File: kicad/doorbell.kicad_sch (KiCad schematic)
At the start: 93 parts, among them J1 USB-C (USB4105), J2 WF26 bus, K1 GAQW212GS, K2 GAQY212GS, K3 GAQY412EH, K4 GAQY412EH, K5 G6K-2F-Y DC12, Q3 2N7002, Q4 2N7002, SW1 BOOT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

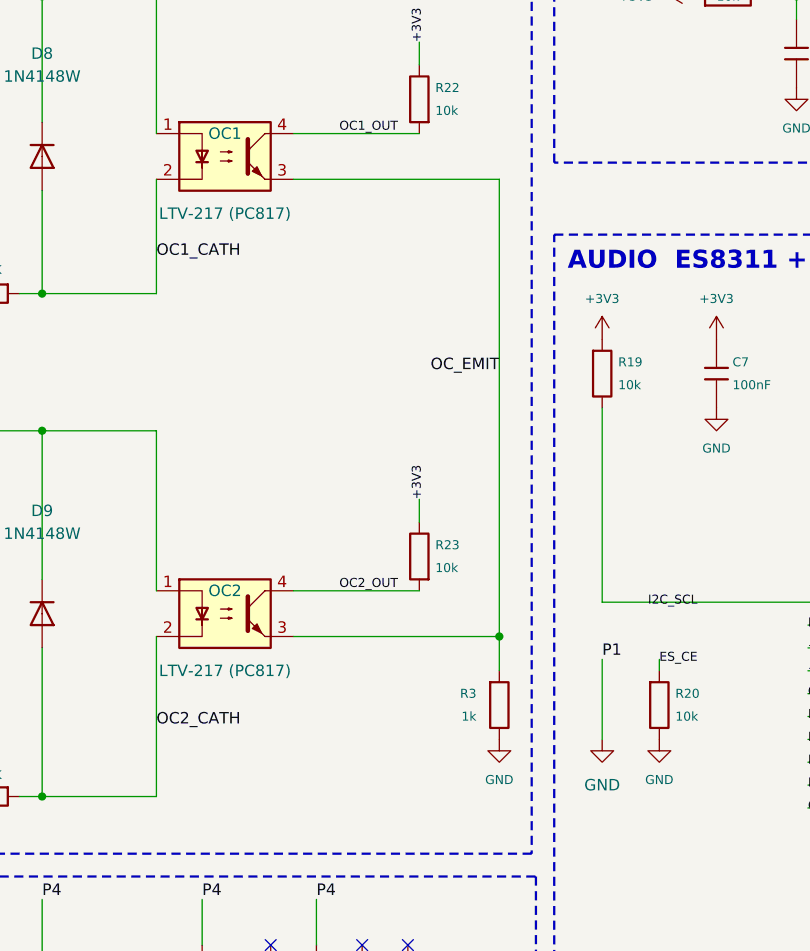
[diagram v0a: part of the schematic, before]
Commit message: kicad: drop R3 shared opto-emitter R, tie OC1/OC2 emitters direct to GND
Removes the 1k shared emitter return for OC1+OC2 (prefab W3). In the
simultaneous-ring corner (front-door Türruf overlapping an apartment Etagenruf
tone) each saturated phototransistor sinks ~0.27 mA, lifting the shared node
~0.54 V and pushing each GPIO LOW to ~0.63-0.91 V — touching the ESP V_IL at
the +5% supply corner. Routing each emitter straight to GND drops every LOW
back to Vce(sat) with no shared node, so detection holds regardless of how many
bells ring at once. PCB rerouted + zones refilled.

Claude-Session: https://claude.ai/code/session_01L7QeT64g2akf3TXKfsuiUZ
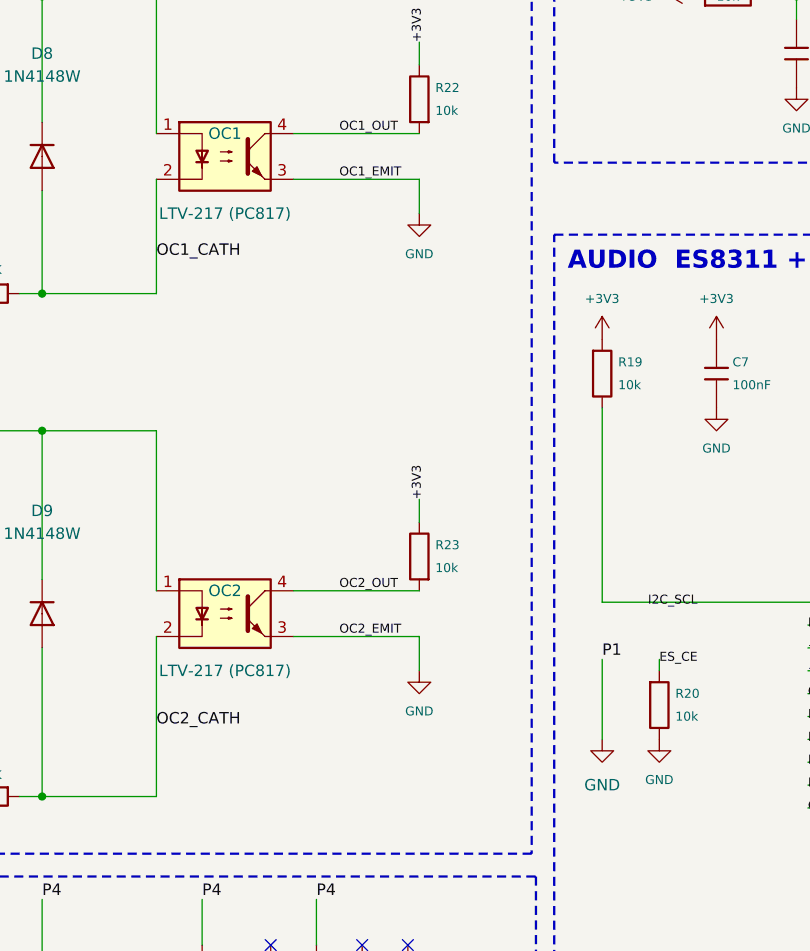
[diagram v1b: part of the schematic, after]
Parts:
- removed R3: 1k, PCM_JLCPCB:R_0603, symbol PCM_JLCPCB-Resistors:0603,1kΩ
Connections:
- net OC_EMIT is gone; now on net GND: OC1.3, OC2.3
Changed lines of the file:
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@@
 	)
 	(junction
-		(at 152.4 184.15)
-		(diameter 0)
-		(color 0 0 0 0)
-	)
-	(junction
 		(at 87.63 247.65)
 		(diameter 0)
@@
 	(wire
 		(pts
-			(xy 152.4 133.35) (xy 152.4 184.15)
-		)
-		(stroke
-			(width 0)
-			(type default)
-		)
-	)
-	(wire
-		(pts
 			(xy 260.35 185.42) (xy 260.35 215.9)
 		)
@@
 	(wire
 		(pts
-			(xy 129.54 184.15) (xy 152.4 184.15)
+			(xy 129.54 184.15) (xy 143.51 184.15)
 		)
 		(stroke
@@
 	(wire
 		(pts
+			(xy 129.54 133.35) (xy 143.51 133.35)
+		)
+		(stroke
+			(width 0)
+			(type default)
+		)
+	)
+	(wire
+		(pts
 			(xy 251.46 190.5) (xy 247.65 190.5)
 		)
@@
 	(wire
 		(pts
+			(xy 143.51 133.35) (xy 143.51 137.16)
+		)
+		(stroke
+			(width 0)
+			(type default)
+		)
+	)
+	(wire
+		(pts
 			(xy 360.68 82.55) (xy 365.76 82.55)
 		)
@@
 	(wire
 		(pts
-			(xy 129.54 133.35) (xy 152.4 133.35)
-		)
-		(stroke
-			(width 0)
-			(type default)
-		)
-	)
-	(wire
-		(pts
 			(xy 119.38 240.03) (xy 119.38 233.68)
 		)
@@
 	(wire
 		(pts
-			(xy 152.4 184.15) (xy 152.4 187.96)
+			(xy 143.51 184.15) (xy 143.51 187.96)
 		)
 		(stroke
@@
 		)
 	)
+	(label "OC2_EMIT"
+		(at 134.62 184.15 0)
+		(effects
+			(font
+				(size 1 1)
+			)
+			(justify bottom)
+		)
+	)
 	(label "+3V3"
 		(at 186.69 185.42 0)
@@
 		)
 	)
-	(label "OC_EMIT"
-		(at 152.4 154.94 180)
-		(effects
-			(font
-				(size 1.27 1.27)
-			)
-			(justify right bottom)
-		)
-	)
 	(label "OC2_CATH"
 		(at 114.3 194.31 0)
@@
 		)
 	)
+	(label "OC1_EMIT"
+		(at 134.62 133.35 0)
+		(effects
+			(font
+				(size 1 1)
+			)
+			(justify bottom)
+		)
+	)
 	(label "OC1_CATH"
 		(at 114.3 142.24 0)
@@
 	)
 	(symbol
+		(lib_id "power:GND")
+		(at 143.51 137.16 0)
+		(mirror y)
+		(unit 1)
+		(body_style 1)
+		(exclude_from_sim no)
+		(in_bom no)
+		(on_board no)
+		(in_pos_files yes)
+		(dnp no)
+		(property "Reference" "#PWR056"
+			(at 143.51 137.16 0)
+			(hide yes)
+			(show_name no)
+			(do_not_autoplace no)
+			(effects
+				(font
+					(size 1 1)
+				)
+			)
+		)
+		(property "Value" "GND"
+			(at 143.51 141.66 0)
+			(show_name no)
+			(do_not_autoplace no)
+			(effects
+				(font
+					(size 1 1)
+				)
+			)
+		)
+		(property "Footprint" ""
+			(at 143.51 137.16 0)
+			(show_name no)
+			(do_not_autoplace no)
+			(effects
+				(font
+					(size 1.27 1.27)
+				)
+			)
+		)
+		(property "Datasheet" ""
+			(at 143.51 137.16 0)
+			(show_name no)
+			(do_not_autoplace no)
+			(effects
+				(font
+					(size 1.27 1.27)
+				)
+			)
+		)
+		(property "Description" ""
+			(at 143.51 137.16 0)
+			(show_name no)
+			(do_not_autoplace no)
+			(effects
+				(font
+					(size 1.27 1.27)
+				)
+			)
+		)
+		(pin "1"
+		)
+		(instances
+			(project "doorbell"
+				(path "/959c5810-086a-4a51-98b0-f68b22907a4f"
+					(reference "#PWR056")
+					(unit 1)
+				)
+			)
+		)
+	)
+	(symbol
 		(lib_id "PCM_JLCPCB-Resistors:0603,22kΩ")
 		(at 242.57 220.98 0)
@@
 	(symbol
 		(lib_id "power:GND")
-		(at 152.4 195.58 0)
+		(at 143.51 187.96 0)
 		(unit 1)
 		(body_style 1)
@@
 		(dnp no)
 		(property "Reference" "#PWR34"
-			(at 152.4 195.58 0)
+			(at 143.51 187.96 0)
 			(hide yes)
 			(show_name no)
@@
 		)
 		(property "Value" "GND"
-			(at 152.4 200.08 0)
+			(at 143.51 192.46 0)
 			(show_name no)
 			(do_not_autoplace no)
@@
 		)
 		(property "Footprint" ""
-			(at 152.4 195.58 0)
+			(at 143.51 187.96 0)
 			(show_name no)
 			(do_not_autoplace no)
@@
 		)
 		(property "Datasheet" ""
-			(at 152.4 195.58 0)
+			(at 143.51 187.96 0)
 			(show_name no)
 			(do_not_autoplace no)
@@
 		)
 		(property "Description" ""
-			(at 152.4 195.58 0)
+			(at 143.51 187.96 0)
 			(show_name no)
 			(do_not_autoplace no)
@@
 					(unit 1)
 				)
-			)
-		)
-	)
-	(symbol
-		(lib_id "PCM_JLCPCB-Resistors:0603,1kΩ")
-		(at 152.4 191.77 0)
-		(unit 1)
-		(body_style 1)
-		(exclude_from_sim no)
-		(in_bom yes)
-		(on_board yes)
-		(in_pos_files yes)
-		(dnp no)
-		(property "Reference" "R3"
-			(at 149.86 190.5 0)
-			(show_name no)
-			(do_not_autoplace no)
-			(effects
-				(font
-					(size 1 1)
-				)
-				(justify right)
-			)
-		)
-		(property "Value" "1k"
-			(at 149.86 193.04 0)
-			(show_name no)
-			(do_not_autoplace no)
-			(effects
-				(font
-					(size 1 1)
-				)
-				(justify right)
-			)
-		)
-		(property "Footprint" "PCM_JLCPCB:R_0603"
-			(at 152.4 191.77 0)
-			(hide yes)
-			(show_name no)
-			(do_not_autoplace no)
-			(effects
-				(font
-					(size 1 1)
-				)
-			)
-		)
-		(property "Datasheet" "https://www.lcsc.com/datasheet/lcsc_datasheet_2206010130_UNI-ROYAL-Uniroyal-Elec-0603WAF1001T5E_C21190.pdf"
-			(at 152.4 191.77 0)
-			(hide yes)
-			(show_name no)
-			(do_not_autoplace no)
-			(effects
-				(font
-					(size 1 1)
-				)
-			)
-		)
-		(property "Description" "Shared opto emitter resistor to GND (uA only)"
-			(at 152.4 191.77 0)
-			(hide yes)
-			(show_name no)
-			(do_not_autoplace no)
-			(effects
-				(font
-					(size 1 1)
-				)
-			)
-		)
-		(property "LCSC" "C21190"
-			(at 152.4 191.77 0)
-			(hide yes)
-			(show_name no)
-			(do_not_autoplace no)
-			(effects
-				(font
-					(size 1 1)
-				)
-			)
-		)
-		(property "MPN" "0603WAF1001T5E"
-			(at 152.4 191.77 0)
-			(hide yes)
-			(show_name no)
-			(do_not_autoplace no)
-			(effects
-				(font
-					(size 1 1)
-				)
-			)
-		)
-		(pin "1"
-		)
-		(pin "2"
-		)
-		(instances
-			(project "doorbell"
-				(path "/959c5810-086a-4a51-98b0-f68b22907a4f"
-					(reference "R3")
-					(unit 1)
-				)

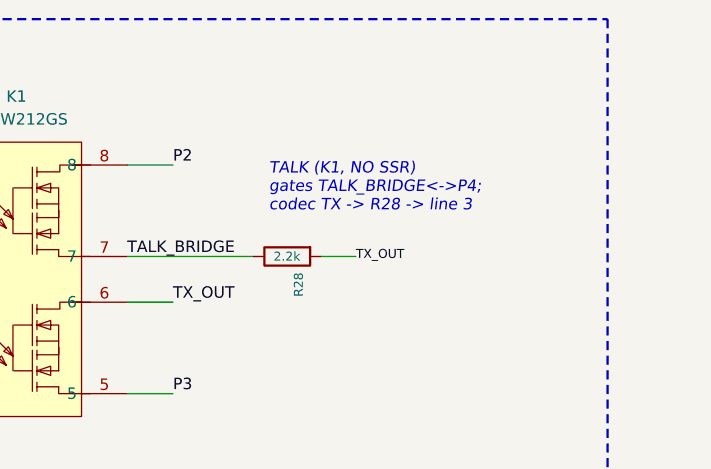
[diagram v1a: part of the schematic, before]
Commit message: kicad: fix W5 doc/tooling drift (TALK annotation + check_pcb no-connect)
- sch: TALK gate annotation TALK_BRIDGE<->P4 -> P2 (matches K1 pole-A nets and its
  own Description); regenerate doorbell.pdf
- doorbell_design.py: drop the vestigial REF identity map and the stale, inert NOCONN
  whitelist. All relay/SSR pads are netted (K1=AQW212 dual, K2/K3=AQY212/AQY412);
  KiCad already names intended no-connects unconnected-(...).
- check_pcb.py: flag any empty-net copper pad directly -- keeps the netlist-omission
  guard with no hand-maintained list; NC intent stays in the schematic's NC flags.
- DESIGN.md / kicad/README.md: correct the doorbell_design.py description (no LCSC
  dict or refdes map; only check_pcb.py imports it; LCSC lives in the schematic symbols).
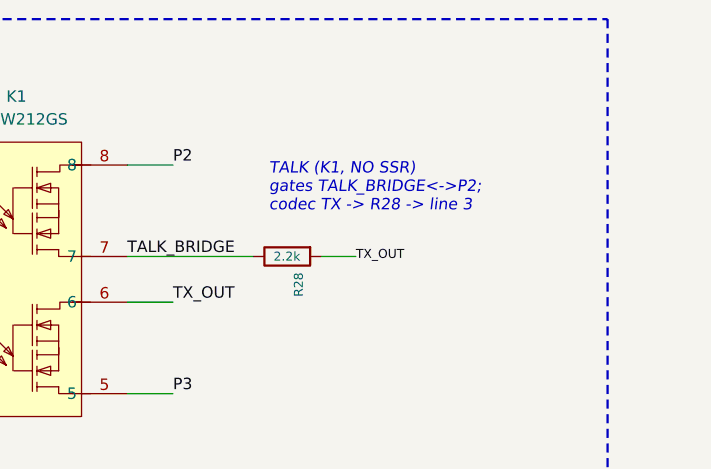
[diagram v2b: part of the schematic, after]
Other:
- note added: "TALK (K1, NO SSR) gates TALK_BRIDGE<->P2; codec TX -> R28 -> line 3"
- note removed: "TALK (K1, NO SSR) gates TALK_BRIDGE<->P4; codec TX -> R28 -> line 3"
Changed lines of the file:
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@@
 		)
 	)
-	(text "TALK (K1, NO SSR)\ngates TALK_BRIDGE<->P4;\ncodec TX -> R28 -> line 3"
+	(text "TALK (K1, NO SSR)\ngates TALK_BRIDGE<->P2;\ncodec TX -> R28 -> line 3"
 		(exclude_from_sim no)
 		(at 357.378 31.75 0)

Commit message: kicad: correct TALK annotation (P2 -> P4)
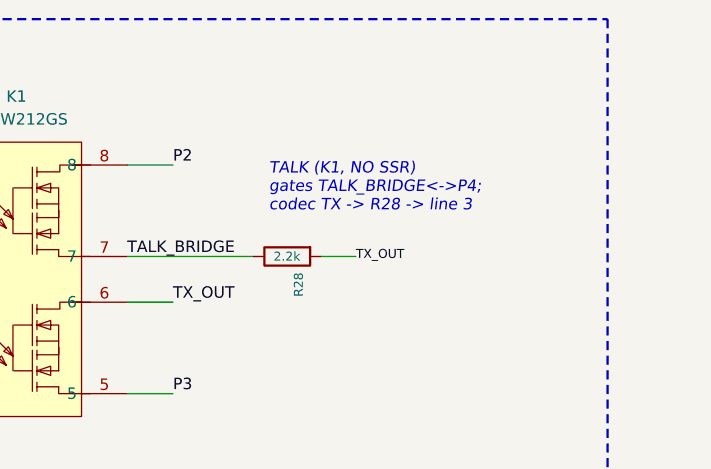
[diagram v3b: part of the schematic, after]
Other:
- note added: "TALK (K1, NO SSR) gates TALK_BRIDGE<->P4; codec TX -> R28 -> line 3"
- note removed: "TALK (K1, NO SSR) gates TALK_BRIDGE<->P2; codec TX -> R28 -> line 3"
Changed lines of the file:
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@@
 		)
 	)
-	(text "TALK (K1, NO SSR)\ngates TALK_BRIDGE<->P2;\ncodec TX -> R28 -> line 3"
+	(text "TALK (K1, NO SSR)\ngates TALK_BRIDGE<->P4;\ncodec TX -> R28 -> line 3"
 		(exclude_from_sim no)
 		(at 357.378 31.75 0)

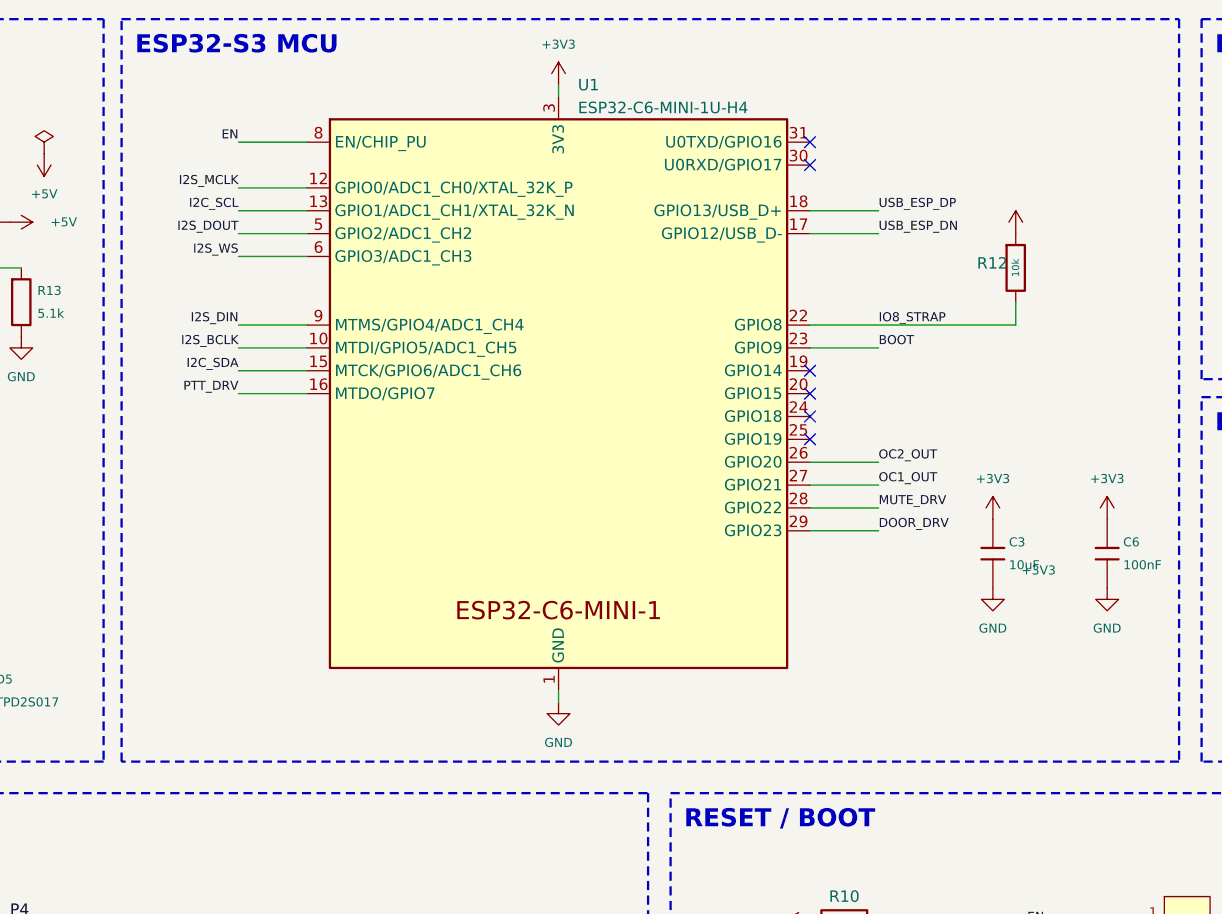
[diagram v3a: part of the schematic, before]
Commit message: kicad+fw+docs: migrate V4 from ESP32-C6 to ESP32-S3-WROOM-1U-N16R8
The single-core C6 starves its WiFi RX under sustained audio load
(pcap-confirmed stream stalls), so audio-over-WiFi never settles. The
dual-core S3 + 8 MB octal PSRAM gives the headroom: audio buffers live in
PSRAM off the internal SRAM, and the WiFi/TLS stack and audio pipeline run
on separate cores.

- kicad: swap U1 ESP32-C6-MINI-1U -> ESP32-S3-WROOM-1U-N16R8 (16 MB flash,
  8 MB PSRAM, u.FL), rewire to the S3 pinout, drop R12, place + reposition
  for the spin. S3 3D model added under kicad/lib_mcu/.
- firmware/doorbell-v4.yaml: board esp32-s3-devkitc-1 / variant esp32s3,
  flash_size 16MB, add psram (octal 80MHz), remap all I2C/I2S/SSR/opto pins.
- DESIGN.md: MCU rationale, GPIO map, V3<->V4 table, and C6/MINI-1U refs
  updated to the S3.

Claude-Session: https://claude.ai/code/session_01L7QeT64g2akf3TXKfsuiUZ
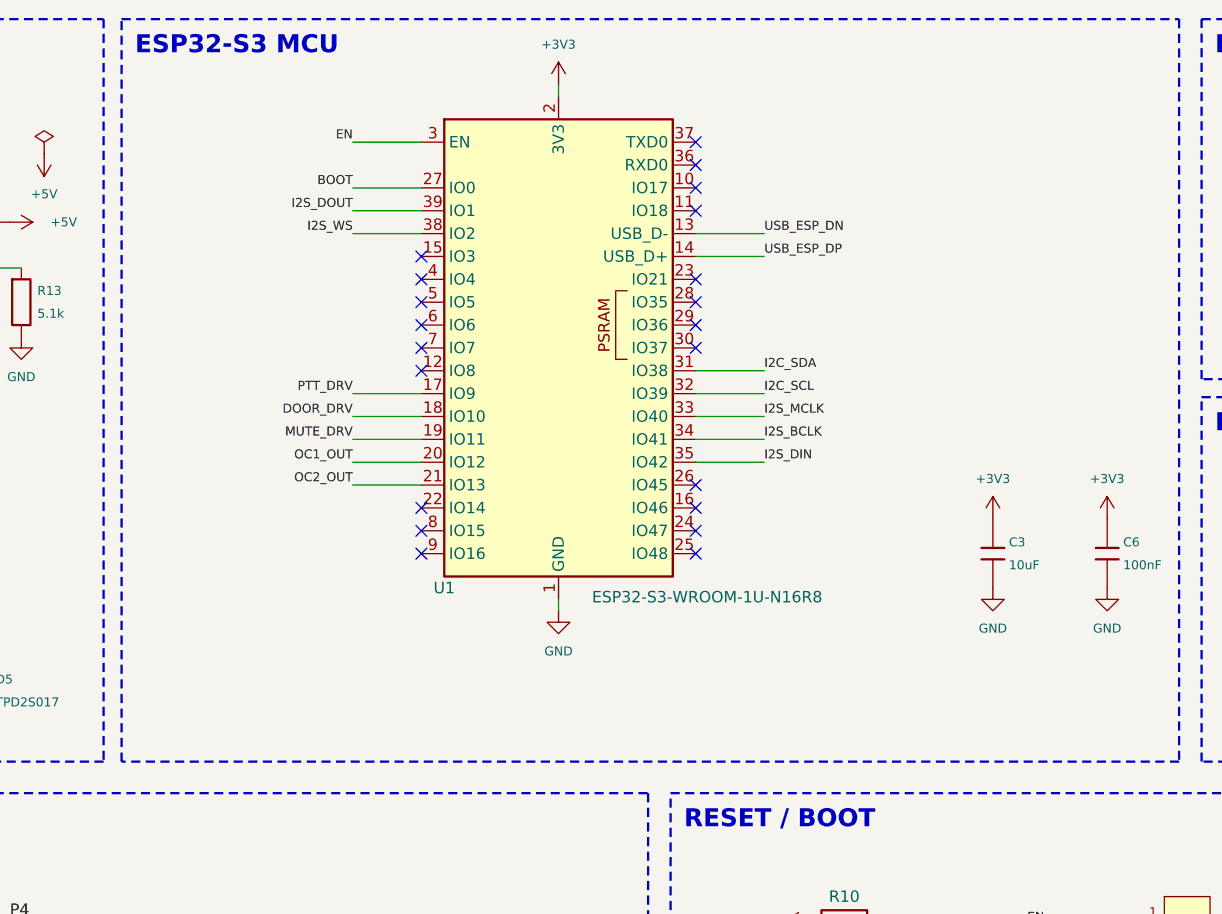
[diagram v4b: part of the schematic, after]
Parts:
- removed R12: 10k, PCM_JLCPCB:R_0402, symbol PCM_JLCPCB-Resistors:0603,10kΩ
- removed U1: ESP32-C6-MINI-1U-H4, PCM_Espressif:ESP32-C6-MINI-1U, symbol PCM_Espressif:ESP32-C6-MINI-1/U
- added U1: ESP32-S3-WROOM-1U-N16R8, RF_Module:ESP32-S3-WROOM-1U, symbol RF_Module:ESP32-S3-WROOM-1
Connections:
- net +3V3: now also U1.2 (3V3)
- net BOOT: now also U1.27 (IO0)
- net DOOR_DRV: now also U1.18 (IO10)
- net EN: now also U1.3 (EN)
- net GND: now also U1.1 (GND), U1.40 (GND), U1.41 (GND)
- net I2C_SCL: now also U1.32 (IO39)
- net I2C_SDA: now also U1.31 (IO38)
- net I2S_BCLK: now also U1.34 (IO41)
- net I2S_DIN: now also U1.35 (IO42)
- net I2S_DOUT: now also U1.39 (IO1)
- net I2S_MCLK: now also U1.33 (IO40)
- net I2S_WS: now also U1.38 (IO2)
- net MUTE_DRV: now also U1.19 (IO11)
- net OC1_OUT: now also U1.20 (IO12)
- net OC2_OUT: now also U1.21 (IO13)
- net PTT_DRV: now also U1.17 (IO9)
- net USB_ESP_DN: now also U1.13 (USB_D-)
- net USB_ESP_DP: now also U1.14 (USB_D+)
- no-connect marks 14 -> 29

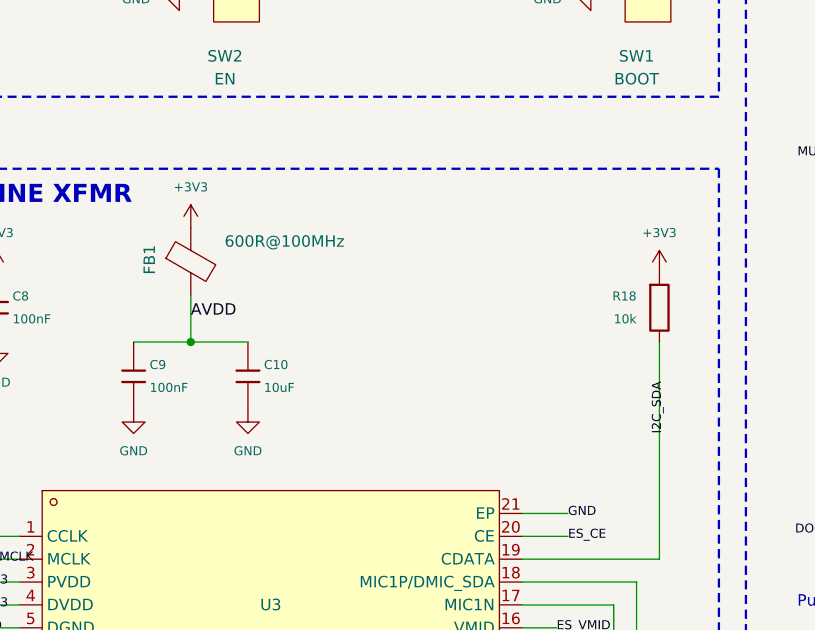
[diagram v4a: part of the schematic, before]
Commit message: audio: dedicated LP5907 LDO (AU_3V3) for ES8311 AVDD
Add U4 LP5907MFX-3.3 off +5V feeding AVDD through FB1; EN tied to +3V3
for digital-before-analog sequencing. PVDD/DVDD stay on +3V3. Update
sch/pcb/DESIGN.md; add WF26 reference photos.

Claude-Session: https://claude.ai/code/session_01L7QeT64g2akf3TXKfsuiUZ
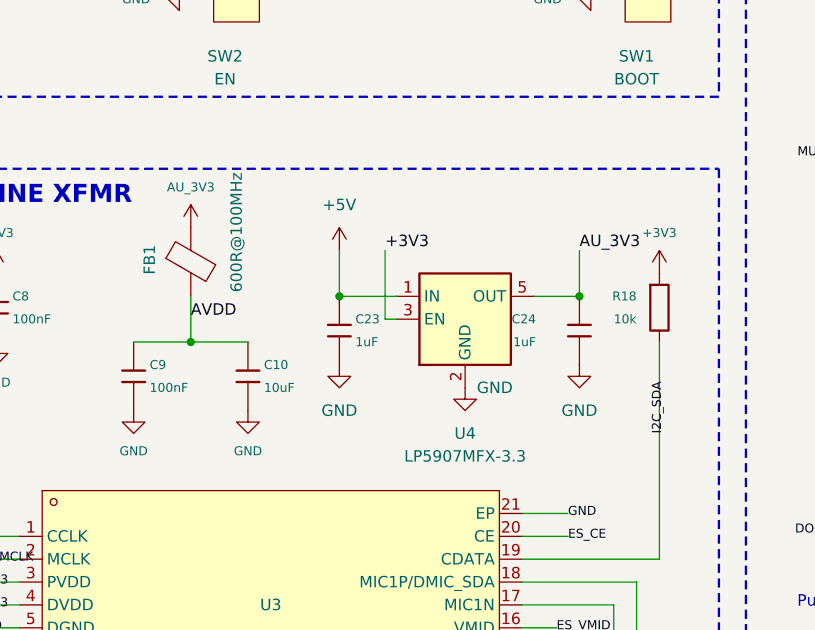
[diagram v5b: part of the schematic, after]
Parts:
- added C23, C24: 1uF, PCM_JLCPCB:C_0603, symbol PCM_JLCPCB-Capacitors:0603,1uF
- added U4: LP5907MFX-3.3, Package_TO_SOT_SMD:SOT-23-5, symbol Regulator_Linear:LP5907MFX-3.3
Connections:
- net +3V3: now also U4.3 (EN); no longer FB1.1
- net +5V: now also C23.1, U4.1 (IN)
- net GND: now also C23.2, C24.2, U4.2 (GND)
- new net AU_3V3: C24.1, FB1.1, U4.5 (OUT)
